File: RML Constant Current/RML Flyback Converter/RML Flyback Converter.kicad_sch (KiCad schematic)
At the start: 4 parts, among them IC1 LT8315IFE#PBF, J1 Tyco, J2 Tyco, J3 447640401

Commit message: rml flyback schematic
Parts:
- removed IC1: LT8315IFE#PBF, LT8630:LT8630IFETRPBF, symbol LT8315IFE#PBF:LT8315IFE#PBF
- added C1: 3.3u, symbol Device:C_US
- added C10, C11, C9: 1u, symbol Device:C
- added C2: 0.47u, symbol Device:C
- added C3: 10pF, symbol Device:C
- added C4, C7, C8: 0.33uF, symbol Device:C
- added C5, C6: 10uF, symbol Device:C
- added D1, D2, D3, D4: D, symbol Device:D
- added D5, D6: D_Zener, symbol Device:D_Zener
- added L1: 1500uH, symbol Device:L
- added Q1: Q_NMOS, symbol Device:Q_NMOS
- added R1: 5k, symbol Device:R_US
- added R10: 100k, symbol Device:R_US
- added R11, R4: 10.7k, symbol Device:R_US
- added R2: 0.33, symbol Device:R_US
- added R3: 22.1k, symbol Device:R_US
- added R5: 1.24k, symbol Device:R_US
- added R6, R7: (no value), symbol Device:R_US
- added R8: 1M, symbol Device:R_US
- added R9: 20k, symbol Device:R_US
- added U1: LT8315HFE-TRPBF, FE_20BB_ADI, symbol LT8315IFE#PBF:LT8315HFE-TRPBF
- added U2: Optocoupler, symbol Isolator:Optocoupler_DC_PhotoNPN_AKEC
- added U3: (no value), Package_SO:SOIC-8_3.9x4.9mm_P1.27mm, symbol Timer:LM555xM
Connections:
- net GND: now also C10.2, C11.1, C9.1, R11.1, U3.1 (GND)
- net GNDPWR: now also D6.2 (A), R7.1, U2.2
- net HVIL+: now also C6.2, C7.2, C8.2, D3.2 (A), D5.1 (K), L1.2
- net HVIL-: now also U2.1
- net RML-: now also Q1.D
- net TS+: now also D1.2 (A)
- new net: C1.1, C2.1, D1.1 (K), R1.2, R6.2, U1.1 (DRAIN), U1.2 (DRAIN), U1.3 (DRAIN)
- new net: C3.2, U1.10 (DCM)
- new net: R4.1, R5.2, U1.12 (FB)
- new net: R3.2, U1.13 (VC)
- new net: C4.1, C5.2, D4.1 (K), L1.1, R2.1, R5.1, U1.14 (IREG/SS), U1.15 (GND), U1.20 (GND), U1.21 (GND)
- new net: C5.1, U1.16 (SMODE), U1.8 (INTVCC)
- new net: D6.1 (K), R6.1, R7.2, U1.17 (EN/UVLO)
- new net: R2.2, U1.18 (SOURCE)
- new net: C6.1, D2.1 (K), U1.9 (BIAS)
- new net: C3.1, R1.1
- new net: Q1.G, R11.2, U2.3
- new net: D2.2 (A), D3.1 (K), R4.2
- new net: C4.2, R3.1
- new net: C11.2, R8.1, U3.2 (TRIG), U3.6 (THRES)
- new net: R8.2, R9.1, U3.7 (DISCH)
- new net: R10.2, U2.4, U3.3 (OUT)
- new net LV+: C10.1, C9.2, R10.1, R9.2, U3.4 (~{RST}), U3.8 (VCC)
- new net TS-: C1.2, C2.2, C7.1, C8.1, D4.2 (A), D5.2 (A)
- no-connect marks 0 -> 2
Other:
- moved on the sheet: J1, J2, J3

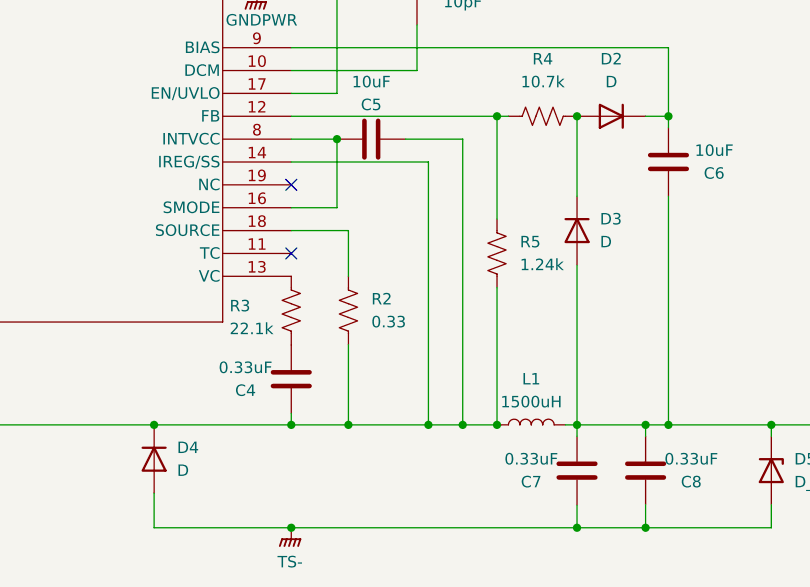
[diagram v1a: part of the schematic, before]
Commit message: added capacitor
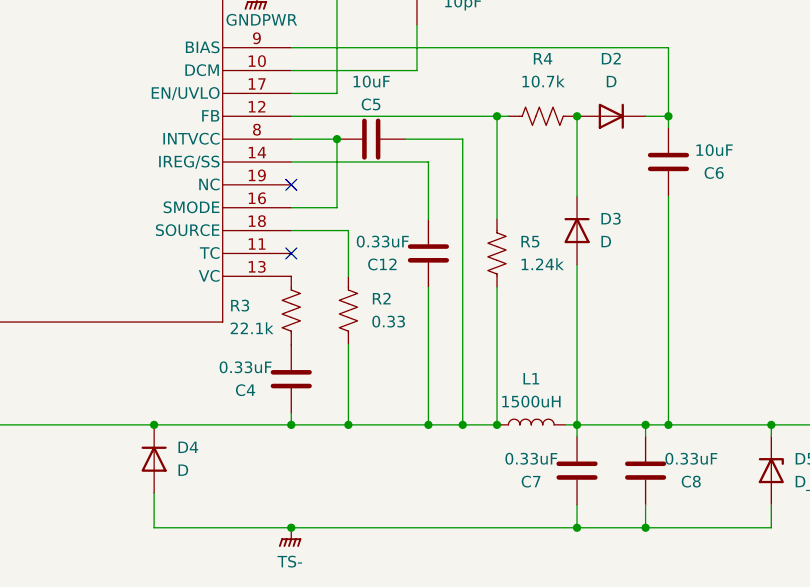
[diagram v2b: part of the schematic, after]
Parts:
- added C12: 0.33uF, symbol Device:C
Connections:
- net at C4.1, C5.2, D4.1 (K)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: now also C12.1; no longer U1.14 (IREG/SS)
- new net: C12.2, U1.14 (IREG/SS)
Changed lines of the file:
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@@
 	)
 	(junction
+		(at 127 128.27)
+		(diameter 0)
+		(color 0 0 0 0)
+	)
+	(junction
 		(at 111.76 128.27)
 		(diameter 0)
@@
 	)
 	(junction
-		(at 127 128.27)
-		(diameter 0)
-		(color 0 0 0 0)
-	)
-	(junction
 		(at 228.6 104.14)
 		(diameter 0)
@@
 	(wire
 		(pts
-			(xy 127 99.06) (xy 127 128.27)
-		)
-		(stroke
-			(width 0)
-			(type default)
-		)
-	)
-	(wire
-		(pts
 			(xy 228.6 109.22) (xy 228.6 116.84)
 		)
@@
 	(wire
 		(pts
+			(xy 127 128.27) (xy 130.81 128.27)
+		)
+		(stroke
+			(width 0)
+			(type default)
+		)
+	)
+	(wire
+		(pts
 			(xy 111.76 127) (xy 111.76 128.27)
 		)
@@
 	(wire
 		(pts
+			(xy 127 113.03) (xy 127 128.27)
+		)
+		(stroke
+			(width 0)
+			(type default)
+		)
+	)
+	(wire
+		(pts
 			(xy 43.18 88.9) (xy 43.18 92.71)
 		)
@@
 	(wire
 		(pts
-			(xy 130.81 128.27) (xy 127 128.27)
+			(xy 111.76 139.7) (xy 143.51 139.7)
 		)
 		(stroke
@@
 	(wire
 		(pts
-			(xy 111.76 139.7) (xy 143.51 139.7)
+			(xy 127 99.06) (xy 127 105.41)
 		)
 		(stroke
@@
 					(unit 1)
 				)
+			)
+		)
+	)
+	(symbol
+		(lib_id "Device:C")
+		(at 127 109.22 180)
+		(unit 1)
+		(body_style 1)
+		(exclude_from_sim no)
+		(in_bom yes)
+		(on_board yes)
+		(in_pos_files yes)
+		(dnp no)
+		(property "Reference" "C12"
+			(at 121.92 110.49 0)
+			(show_name no)
+			(do_not_autoplace no)
+			(effects
+				(font
+					(size 1.27 1.27)
+				)
+			)
+		)
+		(property "Value" "0.33uF"
+			(at 121.92 107.95 0)
+			(show_name no)
+			(do_not_autoplace no)
+			(effects
+				(font
+					(size 1.27 1.27)
+				)
+			)
+		)
+		(property "Footprint" ""
+			(at 126.0348 105.41 0)
+			(hide yes)
+			(show_name no)
+			(do_not_autoplace no)
+			(effects
+				(font
+					(size 1.27 1.27)
+				)
+			)
+		)
+		(property "Datasheet" ""
+			(at 127 109.22 0)
+			(hide yes)
+			(show_name no)
+			(do_not_autoplace no)
+			(effects
+				(font
+					(size 1.27 1.27)
+				)
+			)
+		)
+		(property "Description" "Unpolarized capacitor"
+			(at 127 109.22 0)
+			(hide yes)
+			(show_name no)
+			(do_not_autoplace no)
+			(effects
+				(font
+					(size 1.27 1.27)
+				)
+			)
+		)
+		(pin "1"
+		)
+		(pin "2"
+		)
+		(instances
+			(project "RML Flyback Converter"
+				(path "/3fe68f58-dcb1-40f3-881d-2a06abdc71f5"
+					(reference "C12")
+					(unit 1)
+				)
